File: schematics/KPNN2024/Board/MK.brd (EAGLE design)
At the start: 68.9 x 68.9 mm, 18 parts

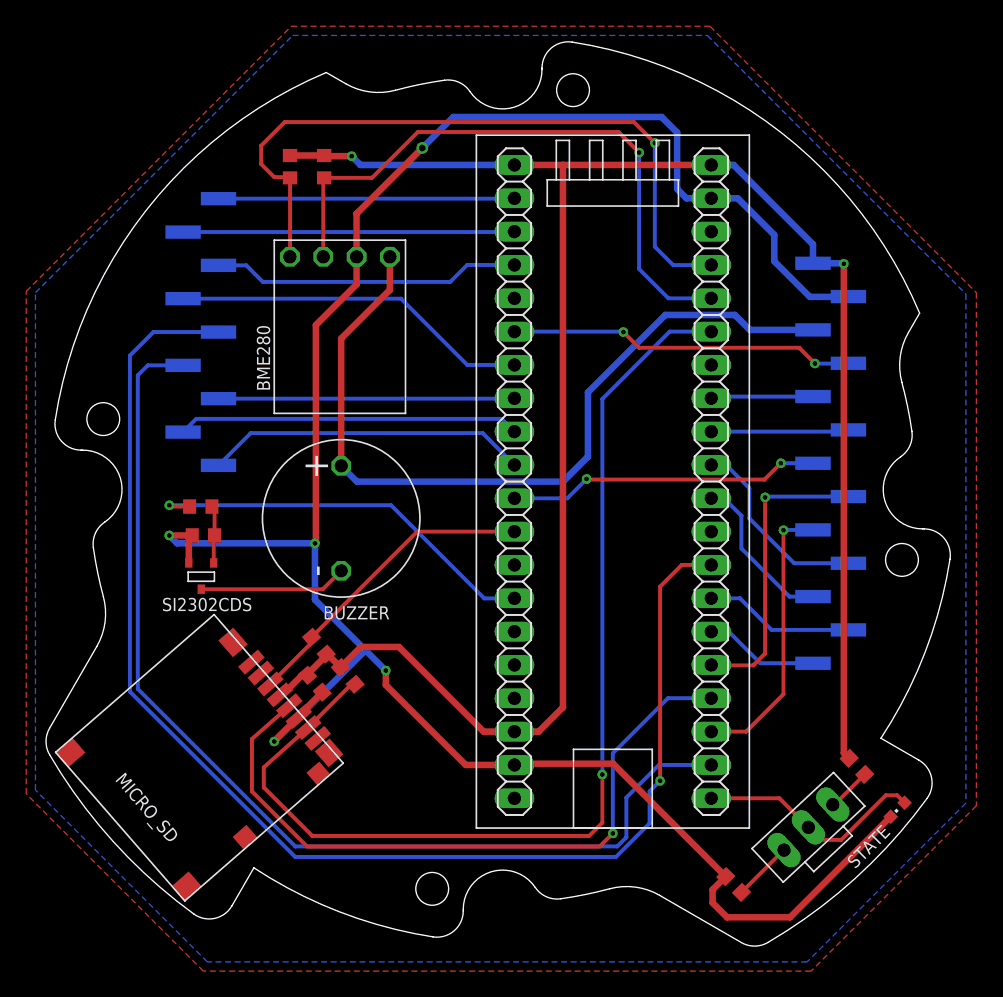
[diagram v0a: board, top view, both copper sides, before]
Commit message: поправила платы
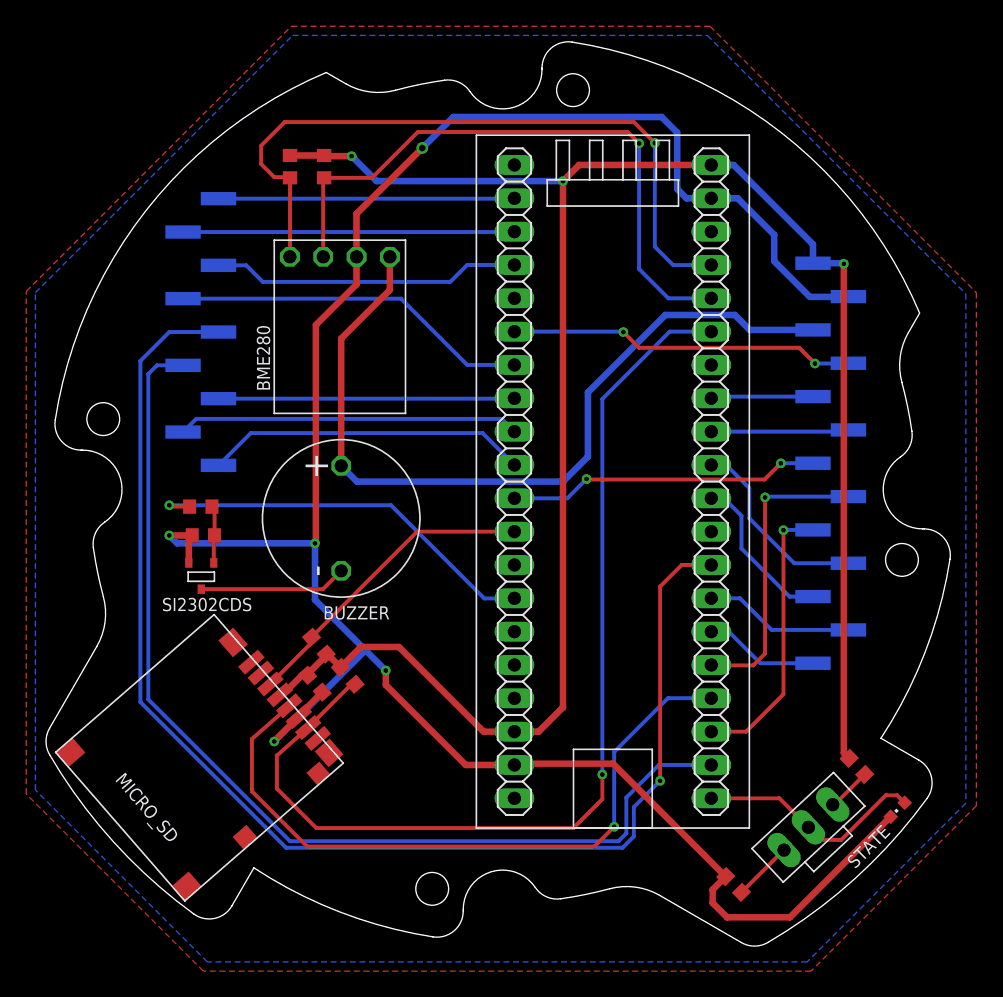
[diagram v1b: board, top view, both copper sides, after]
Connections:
- net 3V3: no longer STM.1
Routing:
- net D0_SD: track 81.5 -> 78.6 mm
- net MISO_RADIO: track 101.9 -> 99.9 mm
- net SCK_RADIO: track 80.7 -> 79.1 mm
- net 3V3: track 153.4 -> 153.2 mm, vias 2 -> 3
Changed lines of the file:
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@@
 <?xml version="1.0" encoding="utf-8"?>
 <!DOCTYPE eagle SYSTEM "eagle.dtd">
-<eagle version="9.6.2">
+<eagle version="9.4.2">
 <drawing>
 <settings>
-<setting alwaysvectorfont="no"/>
+<setting alwaysvectorfont="yes"/>
 <setting verticaltext="up"/>
 </settings>
@@
 </element>
 <element name="BUZZER" library="CanCubeSat" package="BUZZER-S8R12" value="BUZZERS8R6" x="28.7" y="38.8" smashed="yes" rot="R90">
-<attribute name="NAME" x="32.4" y="32.1" size="1" layer="21" ratio="15" rot="R180"/>
+<attribute name="NAME" x="32.4" y="32.1" size="1" layer="25" ratio="15" rot="R180"/>
 </element>
 <element name="SI2302CDS" library="CanCubeSat" package="SOT23-3" value="SI2302CDS" x="18.0376875" y="34.405815625" smashed="yes" rot="R180">
@@
 <contactref element="STM" pad="40"/>
 <contactref element="STM" pad="18"/>
-<contactref element="STM" pad="1"/>
 <contactref element="U$4" pad="1"/>
 <via x="67" y="58.2" extent="1-16" drill="0.35"/>
@@
 <wire x1="33.1" y1="29" x2="39.55" y2="22.55" width="0.5" layer="1"/>
 <wire x1="39.55" y1="22.55" x2="41.9" y2="22.55" width="0.5" layer="1"/>
-<wire x1="56.9" y1="65.73" x2="45.6" y2="65.73" width="0.5" layer="1"/>
 <wire x1="66.96" y1="58.24" x2="67" y2="58.2" width="0.5" layer="16"/>
 <wire x1="67" y1="58.2" x2="67" y2="20.920975" width="0.5" layer="1"/>
@@
 <wire x1="64.65" y1="58.24" x2="64.65" y2="59.68" width="0.5" layer="16"/>
 <wire x1="64.65" y1="59.68" x2="58.6" y2="65.73" width="0.5" layer="16"/>
-<wire x1="41.9" y1="65.73" x2="30.17" y2="65.73" width="0.5" layer="16"/>
-<wire x1="30.17" y1="65.73" x2="29.5" y2="66.4" width="0.5" layer="16"/>
 <via x="29.5" y="66.4" extent="1-16" drill="0.35"/>
 <wire x1="29.5" y1="66.4" x2="27.45" y2="66.4" width="0.5" layer="1"/>
@@
 <wire x1="27.641503125" y1="28.45849375" x2="28.59895625" y2="27.501040625" width="0.5" layer="1"/>
 <wire x1="41.9" y1="22.55" x2="43.75" y2="22.55" width="0.5" layer="1"/>
-<wire x1="45.6" y1="24.4" x2="45.6" y2="65.73" width="0.5" layer="1"/>
+<wire x1="45.6" y1="24.4" x2="45.6" y2="64.5" width="0.5" layer="1"/>
 <wire x1="43.75" y1="22.55" x2="45.6" y2="24.4" width="0.5" layer="1"/>
-<wire x1="45.6" y1="65.73" x2="41.9" y2="65.73" width="0.5" layer="1"/>
+<wire x1="31.4" y1="64.5" x2="45.6" y2="64.5" width="0.5" layer="16"/>
+<via x="45.6" y="64.5" extent="1-16" drill="0.35"/>
+<wire x1="29.5" y1="66.4" x2="31.4" y2="64.5" width="0.5" layer="16"/>
+<wire x1="45.6" y1="64.5" x2="46.83" y2="65.73" width="0.5" layer="1"/>
+<wire x1="46.83" y1="65.73" x2="56.9" y2="65.73" width="0.5" layer="1"/>
 </signal>
 <signal name="SCL">
 <contactref element="STM" pad="36"/>
 <contactref element="BME280" pad="P$2"/>
-<via x="51.4" y="66.6718" extent="1-16" drill="0.35"/>
-<wire x1="49.8298" y1="68.242" x2="51.4" y2="66.6718" width="0.3" layer="1"/>
-<wire x1="51.4" y1="66.6718" x2="51.4" y2="57.8" width="0.3" layer="16"/>
+<via x="51.4" y="67.3718" extent="1-16" drill="0.35"/>
+<wire x1="50.5298" y1="68.242" x2="51.4" y2="67.3718" width="0.3" layer="1"/>
+<wire x1="51.4" y1="67.3718" x2="51.4" y2="57.8" width="0.3" layer="16"/>
 <wire x1="53.63" y1="55.57" x2="56.9" y2="55.57" width="0.3" layer="16"/>
 <wire x1="51.4" y1="57.8" x2="53.63" y2="55.57" width="0.3" layer="16"/>
@@
 <wire x1="27.4" y1="64.75" x2="31.05" y2="64.75" width="0.3" layer="1"/>
 <wire x1="31.05" y1="64.75" x2="34.542" y2="68.242" width="0.3" layer="1"/>
-<wire x1="34.542" y1="68.242" x2="49.8298" y2="68.242" width="0.3" layer="1"/>
+<wire x1="34.542" y1="68.242" x2="50.5298" y2="68.242" width="0.3" layer="1"/>
 </signal>
 <signal name="SDA">
@@
 <wire x1="21.9" y1="21.9923625" x2="21.9" y2="18" width="0.3" layer="1"/>
 <wire x1="21.9" y1="18" x2="26.1" y2="13.8" width="0.3" layer="1"/>
-<wire x1="48.4" y1="13.8" x2="49.4" y2="14.8" width="0.3" layer="1"/>
-<wire x1="48.4" y1="13.8" x2="26.1" y2="13.8" width="0.3" layer="1"/>
-<via x="49.4" y="14.8" extent="1-16" drill="0.35"/>
-<wire x1="49.4" y1="14.8" x2="49.4" y2="20.9" width="0.3" layer="16"/>
-<wire x1="49.4" y1="20.9" x2="53.6" y2="25.1" width="0.3" layer="16"/>
+<wire x1="48" y1="13.8" x2="49.5" y2="15.3" width="0.3" layer="1"/>
+<wire x1="48" y1="13.8" x2="26.1" y2="13.8" width="0.3" layer="1"/>
+<via x="49.5" y="15.3" extent="1-16" drill="0.35"/>
+<wire x1="49.5" y1="15.3" x2="49.5" y2="21" width="0.3" layer="16"/>
+<wire x1="49.5" y1="21" x2="53.6" y2="25.1" width="0.3" layer="16"/>
 <wire x1="53.6" y1="25.1" x2="56.89" y2="25.1" width="0.3" layer="16"/>
 <wire x1="56.89" y1="25.1" x2="56.9" y2="25.09" width="0.3" layer="16"/>
@@
 <contactref element="STM" pad="28"/>
 <contactref element="U$6" pad="5"/>
-<wire x1="19.35" y1="53" x2="14.4" y2="53" width="0.3" layer="16"/>
-<wire x1="14.4" y1="53" x2="12.599109375" y2="51.199109375" width="0.3" layer="16"/>
-<wire x1="12.599109375" y1="51.199109375" x2="12.599109375" y2="25.600890625" width="0.3" layer="16"/>
-<wire x1="25.2" y1="13" x2="12.599109375" y2="25.600890625" width="0.3" layer="16"/>
-<wire x1="53" y1="18.8" x2="52.2" y2="18" width="0.3" layer="16"/>
+<wire x1="19.35" y1="53" x2="15.6" y2="53" width="0.3" layer="16"/>
+<wire x1="15.6" y1="53" x2="13.399109375" y2="50.799109375" width="0.3" layer="16"/>
+<wire x1="13.399109375" y1="50.799109375" x2="13.399109375" y2="24.800890625" width="0.3" layer="16"/>
+<wire x1="24.5" y1="13.7" x2="13.399109375" y2="24.800890625" width="0.3" layer="16"/>
+<wire x1="53" y1="18.8" x2="51" y2="16.8" width="0.3" layer="16"/>
 <via x="53" y="18.8" extent="1-16" drill="0.35"/>
 <wire x1="53" y1="18.8" x2="53" y2="33.6" width="0.3" layer="1"/>
 <wire x1="54.65" y1="35.25" x2="56.9" y2="35.25" width="0.3" layer="1"/>
 <wire x1="53" y1="33.6" x2="54.65" y2="35.25" width="0.3" layer="1"/>
-<wire x1="52.2" y1="15.56305625" x2="49.63694375" y2="13" width="0.3" layer="16"/>
-<wire x1="52.2" y1="18" x2="52.2" y2="15.56305625" width="0.3" layer="16"/>
-<wire x1="49.63694375" y1="13" x2="25.2" y2="13" width="0.3" layer="16"/>
+<wire x1="51" y1="14.56305625" x2="50.13694375" y2="13.7" width="0.3" layer="16"/>
+<wire x1="51" y1="16.8" x2="51" y2="14.56305625" width="0.3" layer="16"/>
+<wire x1="50.13694375" y1="13.7" x2="24.5" y2="13.7" width="0.3" layer="16"/>
 </signal>
 <signal name="SCK_RADIO">
 <contactref element="STM" pad="22"/>
 <contactref element="U$6" pad="4"/>
-<wire x1="16.65" y1="50.46" x2="13.96" y2="50.46" width="0.3" layer="16"/>
-<wire x1="13.96" y1="50.46" x2="13.2" y2="49.7" width="0.3" layer="16"/>
-<wire x1="13.2" y1="25.8" x2="25.2" y2="13.8" width="0.3" layer="16"/>
-<wire x1="50.4282" y1="14.49836875" x2="50.4282" y2="17.5282" width="0.3" layer="16"/>
-<wire x1="25.2" y1="13.8" x2="49.72983125" y2="13.8" width="0.3" layer="16"/>
-<wire x1="49.72983125" y1="13.8" x2="50.4282" y2="14.49836875" width="0.3" layer="16"/>
+<wire x1="16.65" y1="50.46" x2="14.66" y2="50.46" width="0.3" layer="16"/>
+<wire x1="14.66" y1="50.46" x2="14" y2="49.8" width="0.3" layer="16"/>
+<wire x1="14" y1="25" x2="24.8" y2="14.2" width="0.3" layer="16"/>
+<wire x1="50.4282" y1="14.79836875" x2="50.4282" y2="17.5282" width="0.3" layer="16"/>
+<wire x1="24.8" y1="14.2" x2="49.82983125" y2="14.2" width="0.3" layer="16"/>
+<wire x1="49.82983125" y1="14.2" x2="50.4282" y2="14.79836875" width="0.3" layer="16"/>
 <wire x1="52.91" y1="20.01" x2="56.9" y2="20.01" width="0.3" layer="16"/>
-<wire x1="13.2" y1="49.7" x2="13.2" y2="25.8" width="0.3" layer="16"/>
+<wire x1="14" y1="49.8" x2="14" y2="25" width="0.3" layer="16"/>
 <wire x1="50.4282" y1="17.5282" x2="52.91" y2="20.01" width="0.3" layer="16"/>
 </signal>
@@
 <contactref element="MICRO_SD" pad="DAT0"/>
 <wire x1="26.18874375" y1="22.863946875" x2="26.12951875" y2="22.807525" width="0.3" layer="1"/>
-<wire x1="26.12951875" y1="22.807525" x2="22.8" y2="19.824575" width="0.3" layer="1"/>
-<wire x1="22.8" y1="19.824575" x2="22.8" y2="18.3071125" width="0.3" layer="1"/>
-<wire x1="22.8" y1="18.3071125" x2="26.5071125" y2="14.6" width="0.3" layer="1"/>
-<wire x1="26.5071125" y1="14.6" x2="47.5928875" y2="14.6" width="0.3" layer="1"/>
-<wire x1="47.5928875" y1="14.6" x2="48.6" y2="15.6071125" width="0.3" layer="1"/>
-<wire x1="48.6" y1="15.6071125" x2="48.6" y2="19.2818" width="0.3" layer="1"/>
+<wire x1="26.12951875" y1="22.807525" x2="23.8" y2="20.720484375" width="0.3" layer="1"/>
+<wire x1="23.8" y1="20.720484375" x2="23.8" y2="18.2071125" width="0.3" layer="1"/>
+<wire x1="23.8" y1="18.2071125" x2="26.8071125" y2="15.2" width="0.3" layer="1"/>
+<wire x1="26.8071125" y1="15.2" x2="46.3928875" y2="15.2" width="0.3" layer="1"/>
+<wire x1="46.3928875" y1="15.2" x2="48.6" y2="17.4071125" width="0.3" layer="1"/>
+<wire x1="48.6" y1="17.4071125" x2="48.6" y2="19.2818" width="0.3" layer="1"/>
 <via x="48.6" y="19.2818" extent="1-16" drill="0.35"/>
 <wire x1="48.6" y1="19.2818" x2="48.6" y2="47.9" width="0.3" layer="16"/>

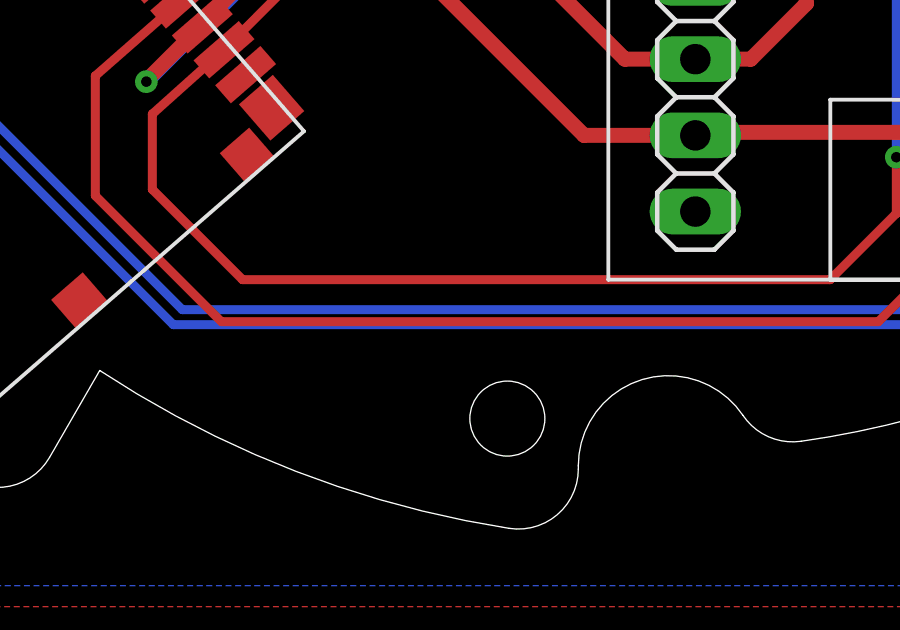
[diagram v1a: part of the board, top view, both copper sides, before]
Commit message: Модели поправлены в соответствии с платами
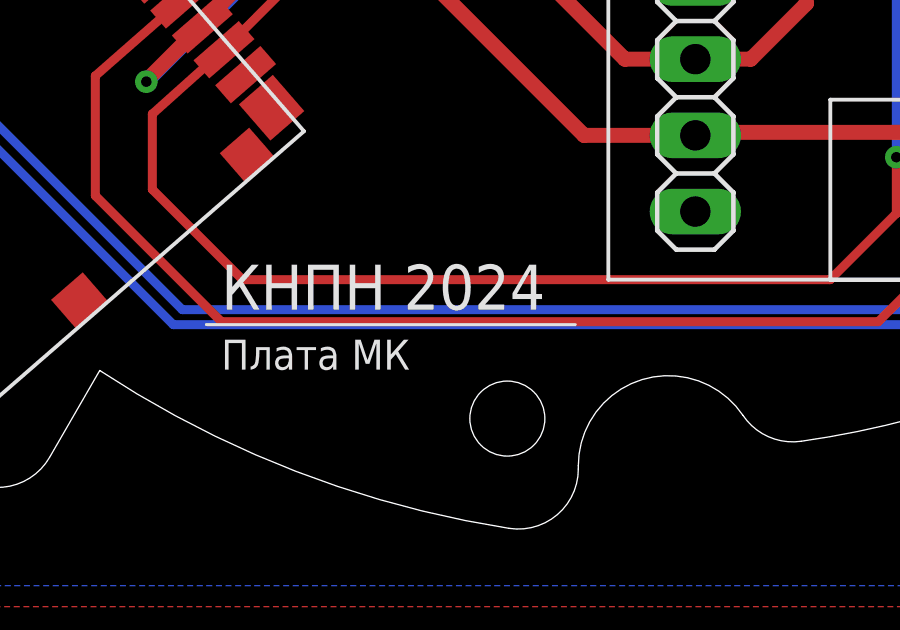
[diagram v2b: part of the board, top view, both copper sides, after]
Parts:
- added U$1: Плата МК, UNKNOWN-2024:LOGO
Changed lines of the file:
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@@
 <attribute name="VALUE" x="70.6509875" y="18.8450625" size="1.27" layer="27" rot="R225"/>
+</element>
+<element name="U$1" library="UNKNOWN-2024" package="LOGO" value="Плата МК" x="25.6" y="13.7" smashed="yes">
+<attribute name="VALUE" x="26.1" y="12.2" size="1" layer="21" font="vector" ratio="15"/>
 </element>
 </elements>
